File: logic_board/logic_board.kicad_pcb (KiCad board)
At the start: 4 copper layers, 80 x 30 mm, 55 parts, among them J1 Debug, J2 Audio In, J3 SJ2-3595X-SMT, J4 Amphenol 124015, J5 Batt, SW1 TL3315NF160Q, SW2 TL3315NF160Q, SW3 TL3315NF160Q, SW4 TL3315NF160Q, SW5 Power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

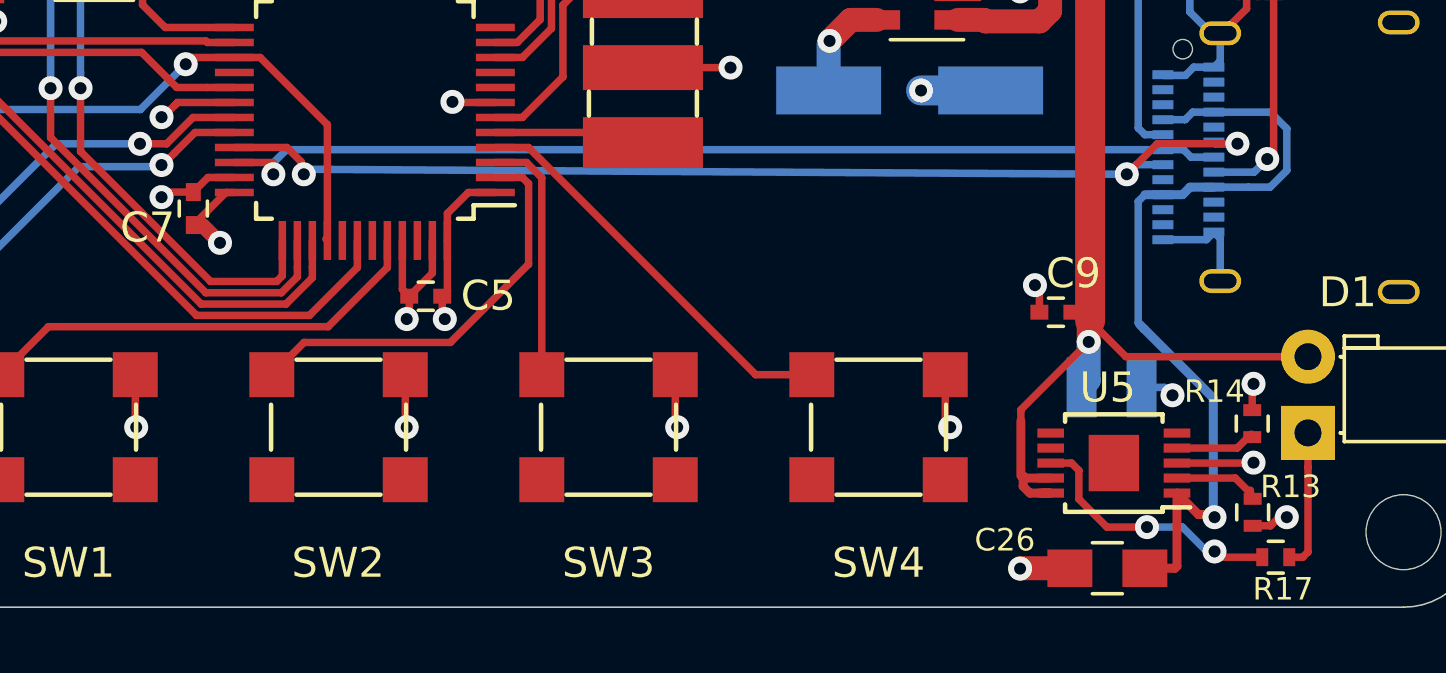
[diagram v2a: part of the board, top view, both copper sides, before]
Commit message: Connect the thermal pad of the charger per datasheet recommendations
- Added a separate pin 11 for the thermal pad in the custom symbol.
- Ground the thermal pad.
- Add a bunch of vias to conduct heat through the board.
- Add a copper pour on the back side of the board to radiate heat.

Although the backside pour is at ground potential, I have added keepouts
around all ground via in its area to avoid ground loops.
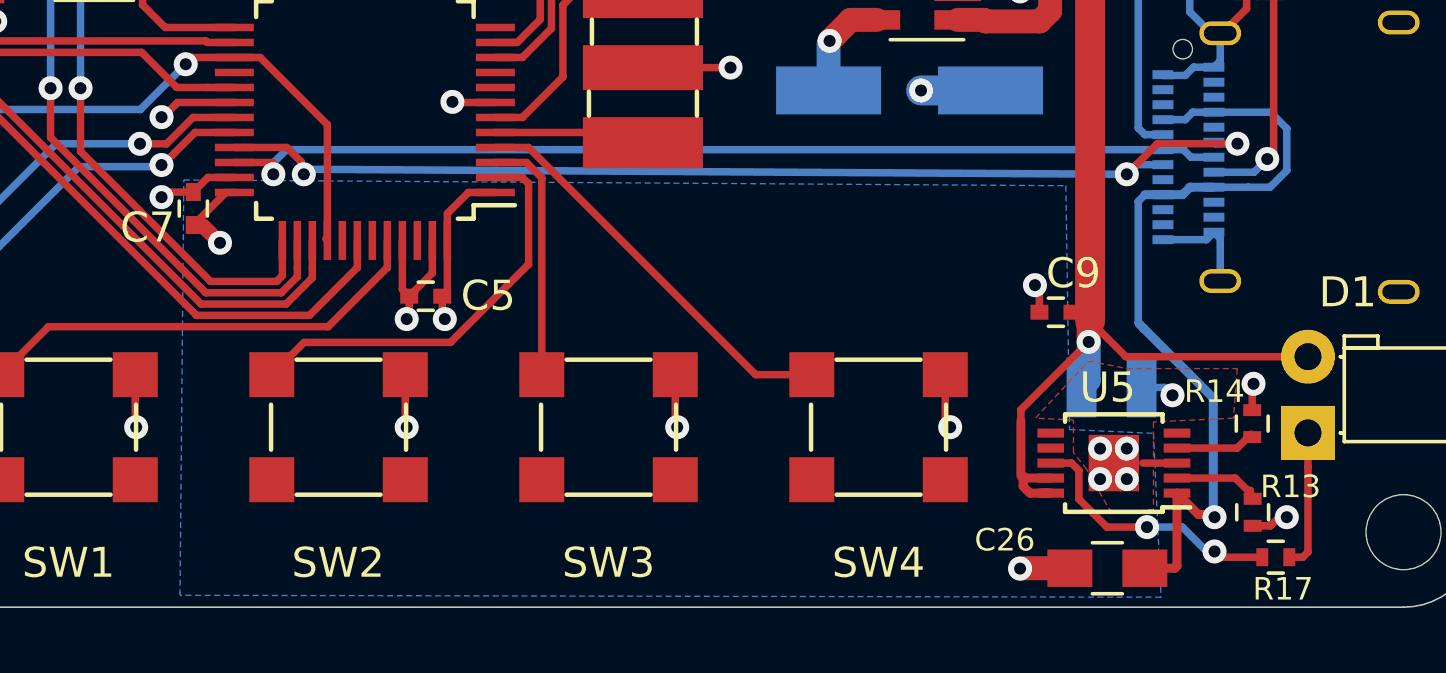
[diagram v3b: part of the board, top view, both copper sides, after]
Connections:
- U5 pad 11: (no net) -> GND
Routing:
- net GND: track 92.2 -> 90.7 mm, vias 33 -> 36
- added copper zone on B.Cu, net GND
- added copper zone on F.Cu, net GND
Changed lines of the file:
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@@
     (thickness 1.6)
     (drawings 21)
-    (tracks 546)
+    (tracks 548)
     (zones 0)
     (modules 55)
@@
       (net 3 +BATT))
     (pad 11 smd rect (at 0.42 0.47 180) (size 0.84 0.94) (layers F.Cu F.Paste F.Mask)
-      (solder_paste_margin_ratio -0.2))
+      (net 2 GND) (solder_paste_margin_ratio -0.2))
     (pad 11 smd rect (at 0.42 -0.47 180) (size 0.84 0.94) (layers F.Cu F.Paste F.Mask)
-      (solder_paste_margin_ratio -0.2))
+      (net 2 GND) (solder_paste_margin_ratio -0.2))
     (pad 11 smd rect (at -0.42 0.47 180) (size 0.84 0.94) (layers F.Cu F.Paste F.Mask)
-      (solder_paste_margin_ratio -0.2))
+      (net 2 GND) (solder_paste_margin_ratio -0.2))
     (pad 11 smd rect (at -0.42 -0.47 180) (size 0.84 0.94) (layers F.Cu F.Paste F.Mask)
-      (solder_paste_margin_ratio -0.2))
+      (net 2 GND) (solder_paste_margin_ratio -0.2))
     (model ${KISYS3DMOD}/Housings_SSOP.3dshapes/MSOP-10-1EP_3x3mm_Pitch0.5mm.wrl
       (at (xyz 0 0 0))
@@
   (segment (start 145.054 105.557) (end 145.034 105.537) (width 0.8) (layer F.Cu) (net 1))
   (segment (start 145.054 106.807) (end 145.054 105.557) (width 0.8) (layer F.Cu) (net 1))
+  (via (at 168.275 124.714) (size 0.8) (drill 0.4) (layers F.Cu B.Cu) (net 2))
+  (via (at 168.275 125.73) (size 0.8) (drill 0.4) (layers F.Cu B.Cu) (net 2))
+  (via (at 167.386 125.73) (size 0.8) (drill 0.4) (layers F.Cu B.Cu) (net 2))
+  (via (at 167.386 124.714) (size 0.8) (drill 0.4) (layers F.Cu B.Cu) (net 2))
   (via (at 155.067 112.014) (size 0.8) (drill 0.4) (layers F.Cu B.Cu) (net 2))
   (via (at 162.38728 124) (size 0.8) (drill 0.4) (layers F.Cu B.Cu) (net 2))
@@
   (segment (start 120.7428 120.2983) (end 120.6754 120.2309) (width 0.5) (layer B.Cu) (net 2))
   (segment (start 121.7295 120.2983) (end 120.7428 120.2983) (width 0.5) (layer B.Cu) (net 2) (status 10))
-  (via (at 172.5 125.182302) (size 0.8) (drill 0.4) (layers F.Cu B.Cu) (net 2))
-  (segment (start 172.49041 125.1966) (end 172.504708 125.182302) (width 0.25) (layer F.Cu) (net 2))
-  (segment (start 169.9482 125.1966) (end 172.49041 125.1966) (width 0.25) (layer F.Cu) (net 2) (status 10))
   (via (at 165.2143 119.2657) (size 0.8) (drill 0.4) (layers F.Cu B.Cu) (net 2))
   (segment (start 165.3628 119.4142) (end 165.2143 119.2657) (width 0.25) (layer F.Cu) (net 2))
@@
   (segment (start 152.9639 100.8559) (end 152.908 100.8) (width 1) (layer B.Cu) (net 2))
   (segment (start 152.9639 103.4161) (end 152.9639 100.8559) (width 1) (layer B.Cu) (net 2))
+  (segment (start 169.9482 125.1966) (end 168.8084 125.1966) (width 0.25) (layer F.Cu) (net 2))
   (segment (start 165 106.25) (end 167.053301 108.303301) (width 1) (layer F.Cu) (net 3))
   (segment (start 166.4628 120.1674) (end 166.7637 120.1674) (width 0.4) (layer F.Cu) (net 3) (status 10))
@@
       )
     )
+  )
+  (zone (net 2) (net_name GND) (layer B.Cu) (hatch edge 0.508)
+    (connect_pads (clearance 0.508))
+    (min_thickness 0.254)
+    (fill yes (arc_segments 32) (thermal_gap 0.508) (thermal_bridge_width 0.508))
+    (polygon
+      (pts
+        (xy 166.37 124.079) (xy 169.164 124.206) (xy 169.418 129.667) (xy 136.7155 129.6035) (xy 136.8425 115.7605)
+        (xy 166.243 115.951)
+      )
+    )
+  )
+  (zone (net 0) (net_name "") (layers F&B.Cu) (hatch edge 0.508)
+    (connect_pads (clearance 0.508))
+    (min_thickness 0.254)
+    (keepout (tracks allowed) (vias allowed) (copperpour not_allowed))
+    (fill (arc_segments 32) (thermal_gap 0.508) (thermal_bridge_width 0.508))
+    (polygon
+      (pts
+        (xy 163.322 124.968) (xy 161.163 124.968) (xy 161.163 123.063) (xy 163.322 123.063)
+      )
+    )
+  )
+  (zone (net 0) (net_name "") (layer B.Cu) (hatch edge 0.508)
+    (connect_pads (clearance 0.508))
+    (min_thickness 0.254)
+    (keepout (tracks allowed) (vias allowed) (copperpour not_allowed))
+    (fill (arc_segments 32) (thermal_gap 0.508) (thermal_bridge_width 0.508))
+    (polygon
+      (pts
+        (xy 154.432 124.9045) (xy 152.146 124.9045) (xy 152.146 122.9995) (xy 154.432 122.9995)
+      )
+    )
+  )
+  (zone (net 0) (net_name "") (layers F&B.Cu) (hatch edge 0.508)
+    (connect_pads (clearance 0.508))
+    (min_thickness 0.254)
+    (keepout (tracks allowed) (vias allowed) (copperpour not_allowed))
+    (fill (arc_segments 32) (thermal_gap 0.508) (thermal_bridge_width 0.508))
+    (polygon
+      (pts
+        (xy 145.415 124.968) (xy 143.002 124.968) (xy 143.002 122.936) (xy 145.415 122.936)
+      )
+    )
+  )
+  (zone (net 0) (net_name "") (layers F&B.Cu) (hatch edge 0.508)
+    (connect_pads (clearance 0.508))
+    (min_thickness 0.254)
+    (keepout (tracks allowed) (vias allowed) (copperpour not_allowed))
+    (fill (arc_segments 32) (thermal_gap 0.508) (thermal_bridge_width 0.508))
+    (polygon
+      (pts
+        (xy 166.497 120.269) (xy 164.211 120.269) (xy 164.211 118.491) (xy 166.4335 118.491)
+      )
+    )
+  )
+  (zone (net 0) (net_name "") (layers F&B.Cu) (hatch edge 0.508)
+    (connect_pads (clearance 0.508))
+    (min_thickness 0.254)
+    (keepout (tracks allowed) (vias allowed) (copperpour not_allowed))
+    (fill (arc_segments 32) (thermal_gap 0.508) (thermal_bridge_width 0.508))
+    (polygon
+      (pts
+        (xy 165.608 129.413) (xy 163.83 129.413) (xy 163.83 127.889) (xy 165.608 127.889)
+      )
+    )
+  )
+  (zone (net 0) (net_name "") (layer B.Cu) (hatch edge 0.508)
+    (connect_pads (clearance 0.508))
+    (min_thickness 0.254)
+    (keepout (tracks allowed) (vias allowed) (copperpour not_allowed))
+    (fill (arc_segments 32) (thermal_gap 0.508) (thermal_bridge_width 0.508))
+    (polygon
+      (pts
+        (xy 145.034 121.158) (xy 143.51 121.158) (xy 143.51 119.634) (xy 145.034 119.634)
+      )
+    )
+  )
+  (zone (net 2) (net_name GND) (layer F.Cu) (hatch edge 0.508)
+    (connect_pads yes (clearance 0.508))
+    (min_thickness 0.254)
+    (fill yes (arc_segments 32) (thermal_gap 0.508) (thermal_bridge_width 0.508))
+    (polygon
+      (pts
+        (xy 168.275 122.047) (xy 171.958 122.047) (xy 171.831 123.698) (xy 169.164 123.825) (xy 169.164 126.746)
+        (xy 167.767 126.873) (xy 166.9415 125.4125) (xy 166.497 124.841) (xy 166.497 123.7615) (xy 165.227 123.698)
+        (xy 167.005 121.793)
+      )
+    )

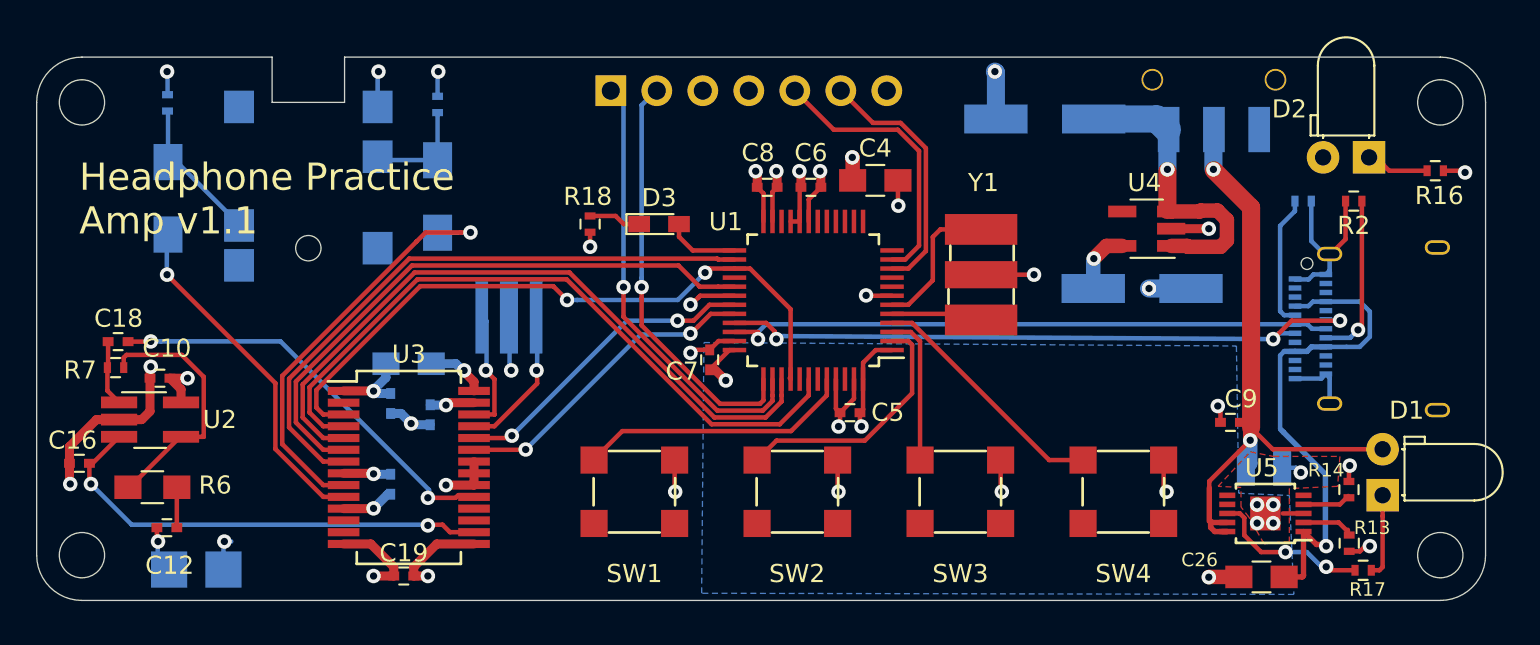
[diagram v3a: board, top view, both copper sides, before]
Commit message: Make C25 a no-stuff, and other layout improvements
C25 was a leftover from when there was a switching regulator.
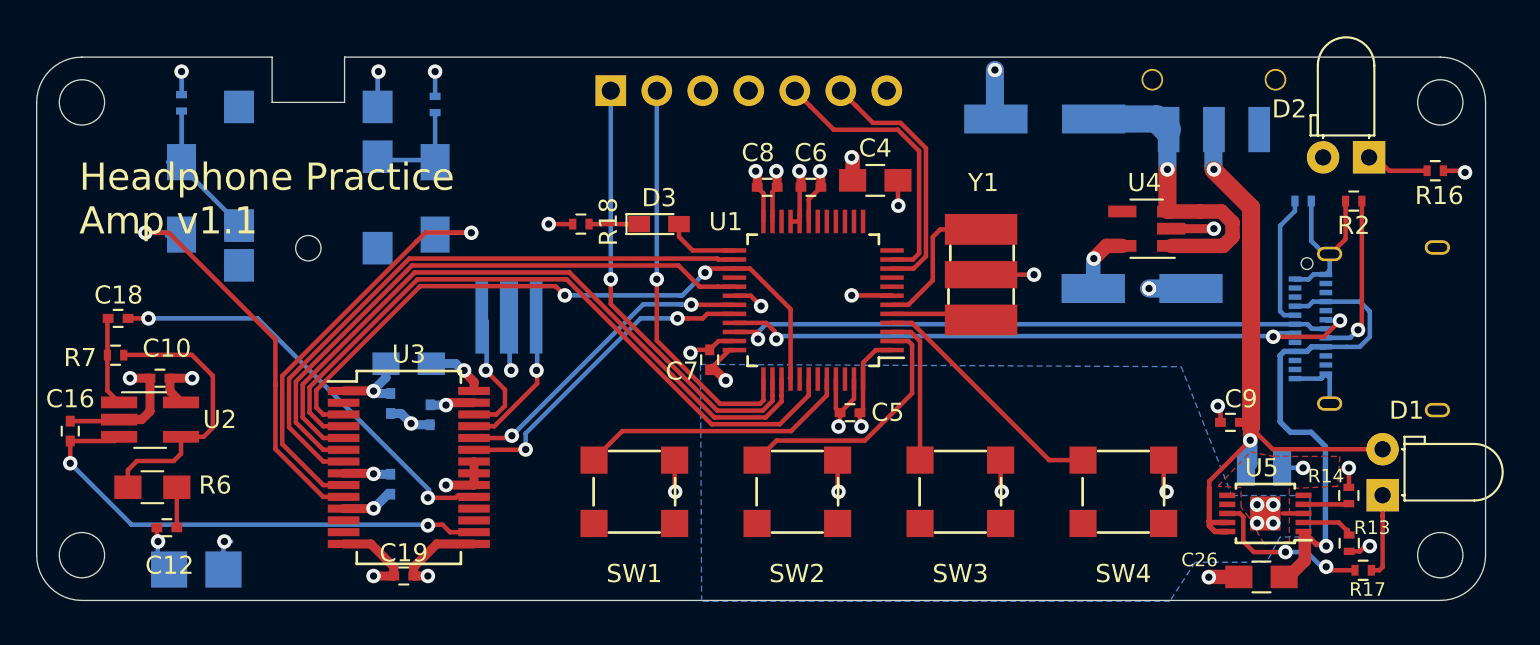
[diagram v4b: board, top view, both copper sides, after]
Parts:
- moved C16 1.85 mm to (101.9, 120.7), turned to 90 degrees
- moved C18 1.28 mm to (104.5, 114.4)
- moved R10 0.77 mm to (108.0, 102.5)
- moved C24 0.75 mm to (108.0, 107.8)
- moved R7 0.69 mm to (104.4, 116.5)
- moved R18 0.51 mm to (130.0, 109.2), turned to 180 degrees
- moved R14 0.33 mm to (172.4, 124.2)
- moved C23 0.17 mm to (122.0, 107.8)
- moved R9 0.14 mm to (122.0, 102.6)
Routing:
- net Net-(C24-Pad1): track 19.4 -> 22.0 mm
- net Net-(C16-Pad1): track 25.7 -> 27.9 mm
- net Net-(C18-Pad1): track 3.64 -> 4.92 mm
- net Net-(R6-Pad1): track 14.3 -> 15.5 mm
- net GND: track 90.7 -> 89.8 mm, vias 36 -> 35
- net Net-(U1-Pad30): track 2.59 -> 1.77 mm
- net +3V3: track 38.4 -> 39.2 mm
- net Net-(J1-Pad2): track 23.2 -> 22.5 mm
- net Net-(U3-Pad26): track 6.83 -> 7.37 mm
- net Net-(C18-Pad2): track 23.1 -> 23.6 mm
- net SDA: track 17.5 -> 18.0 mm
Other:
- board text added: "For Rework"

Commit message: Update to symbols from newest KiCad
LEDs were also on the wrong side of the board.
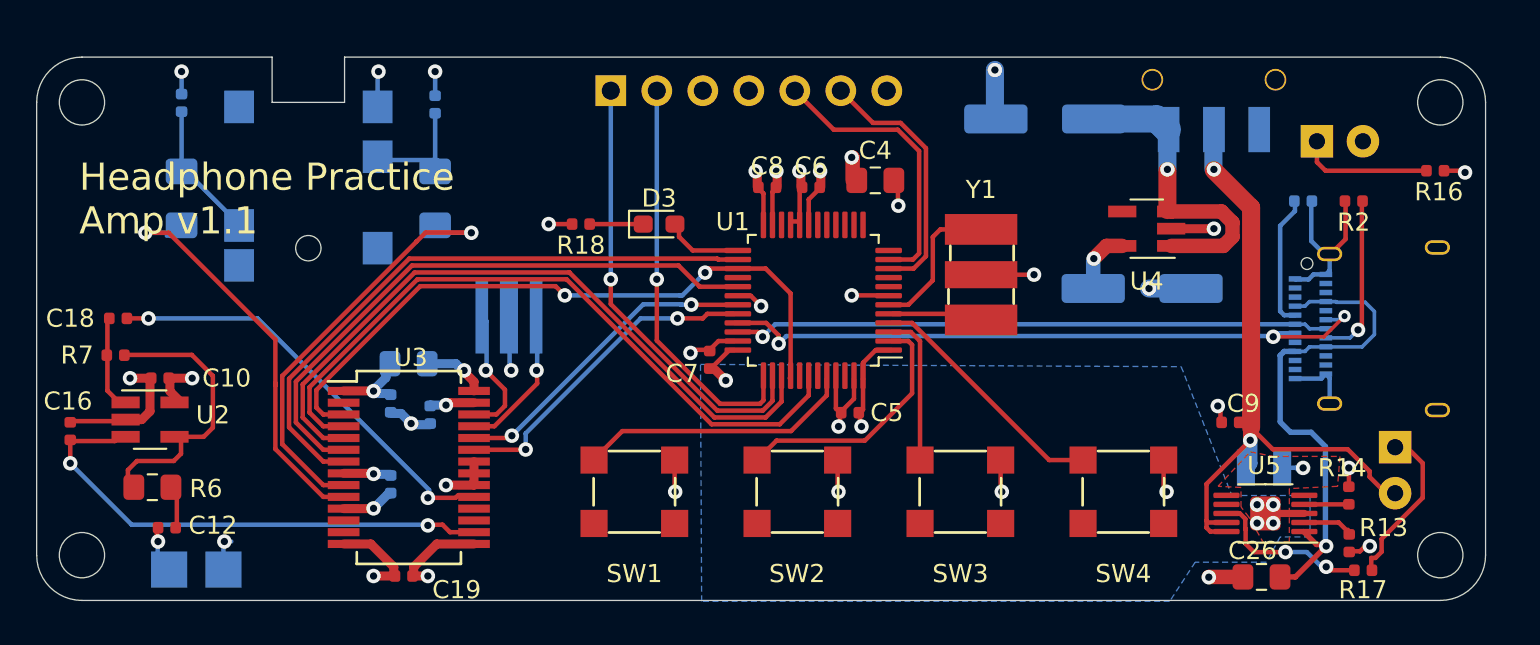
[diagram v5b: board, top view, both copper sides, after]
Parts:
- C10, C12, C15, C16, C17, C18, C19, C20, C5, C6, C7, C8, C9: footprint Capacitors_SMD:C_0402 -> Capacitor_SMD:C_0402_1005Metric
- C13, C26, C4: footprint Capacitors_SMD:C_0805_HandSoldering -> Capacitor_SMD:C_0805_2012Metric_Pad1.15x1.40mm_HandSolder
- C23, C24: footprint Capacitors_SMD:C_1206_HandSoldering -> Capacitor_SMD:C_1206_3216Metric_Pad1.42x1.75mm_HandSolder
- C25, C3: footprint Capacitors_SMD:CP_Elec_6.3x4.5 -> Capacitor_SMD:CP_Elec_6.3x4.5
- D1, D2: footprint LEDs:LED_D3.0mm_Horizontal_O1.27mm_Z2.0mm -> LED_THT:LED_D3.0mm_Horizontal_O1.27mm_Z2.0mm; moved to B.Cu
- D3: footprint LEDs:LED_0603_HandSoldering -> LED_SMD:LED_0603_1608Metric_Pad1.05x0.95mm_HandSolder
- J1: footprint Pin_Headers:Pin_Header_Straight_1x07_Pitch2.54mm -> Connector_PinHeader_2.54mm:PinHeader_1x07_P2.54mm_Vertical
- J4: footprint Connectors_USB:USB_C_Receptacle_Amphenol_12401610E4-2A -> Connector_USB:USB_C_Receptacle_Amphenol_12401610E4-2A
- R1, R10, R13, R14, R16, R17, R18, R2, R7, R9: footprint Resistors_SMD:R_0402 -> Resistor_SMD:R_0402_1005Metric
- R6: footprint Resistors_SMD:R_0805_HandSoldering -> Resistor_SMD:R_0805_2012Metric_Pad1.15x1.40mm_HandSolder
- U1: footprint Housings_QFP:LQFP-48_7x7mm_Pitch0.5mm -> Package_QFP:LQFP-48_7x7mm_P0.5mm
- U2: footprint TO_SOT_Packages_SMD:TSOT-23-5_HandSoldering -> Package_TO_SOT_SMD:SOT-23-5_HandSoldering
- U3: footprint Housings_SSOP:SSOP-28_5.3x10.2mm_Pitch0.65mm -> Package_SO:SSOP-28_5.3x10.2mm_P0.65mm
- U4: footprint TO_SOT_Packages_SMD:SOT-23-5_HandSoldering -> Package_TO_SOT_SMD:SOT-23-5_HandSoldering
- U5: footprint Housings_SSOP:MSOP-10-1EP_3x3mm_Pitch0.5mm -> Package_SO:MSOP-10-1EP_3x3mm_P0.5mm_EP1.68x1.88mm
- moved D2 3.01 mm to (170.7, 104.6), turned to 0 degrees
- moved D1 2.74 mm to (175.0, 121.5), turned to 270 degrees
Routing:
- net Net-(D1-Pad1): track 4.66 -> 9.62 mm
- net Net-(D2-Pad1): track 3.21 -> 7.39 mm
- net +BATT: track 35.8 -> 37.0 mm
- net USB_DM: track 36.3 -> 37.5 mm
- net GND: track 89.8 -> 90.8 mm
- net Net-(C26-Pad1): track 27.6 -> 28.5 mm
- net USB_DP: track 32.9 -> 33.5 mm
- net BCLK: track 36.9 -> 37.4 mm
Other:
- net class Default: trace_width 0.25 -> 0.127; via_dia 0.8 -> 0.4572; via_drill 0.4 -> 0.254
- rule trace_min: 0.2 -> 0.127
